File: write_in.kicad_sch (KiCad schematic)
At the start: 11 parts, among them J3 Bus_PCI_Express_x16, U30 74LS30, U31 74LS00, U32 74LS00

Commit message: Current progress.  Working on laying out the latched bus.
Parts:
- added C2: 100 nF, Capacitor_SMD:C_0805_2012Metric_Pad1.18x1.45mm_HandSolder, symbol Device:C
- added JP16: SolderJumper_3_Open, Jumper:SolderJumper-3_P1.3mm_Open_RoundedPad1.0x1.5mm, symbol Jumper:SolderJumper_3_Open
- added unit 2 of U3
- C1: renamed from C29; footprint (none) -> Capacitor_SMD:C_0805_2012Metric_Pad1.18x1.45mm_HandSolder
- C3: renamed from C30; footprint (none) -> Capacitor_SMD:C_0805_2012Metric_Pad1.18x1.45mm_HandSolder
- JP1: renamed from JP11; footprint (none) -> Jumper:SolderJumper-3_P1.3mm_Open_RoundedPad1.0x1.5mm
- JP2: renamed from JP12; footprint (none) -> Jumper:SolderJumper-3_P1.3mm_Open_RoundedPad1.0x1.5mm
- JP3: renamed from JP13; footprint (none) -> Jumper:SolderJumper-3_P1.3mm_Open_RoundedPad1.0x1.5mm
- JP4: renamed from JP14; footprint (none) -> Jumper:SolderJumper-3_P1.3mm_Open_RoundedPad1.0x1.5mm
- JP5: renamed from JP15; footprint (none) -> Jumper:SolderJumper-3_P1.3mm_Open_RoundedPad1.0x1.5mm
- U1: renamed from U31; footprint (none) -> Package_SO:SOIC-14_3.9x8.7mm_P1.27mm
- U2: renamed from U32; footprint (none) -> Package_SO:SOIC-14_3.9x8.7mm_P1.27mm
- U3: renamed from U30; footprint (none) -> Package_SO:SOIC-14_3.9x8.7mm_P1.27mm
- renumbered J3 to J1
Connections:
- net +3V3: now also C2.1, U3.14 (VCC)
- net GND: now also C2.2, JP16.1 (A), U3.7 (GND)
- net ~{RST}: now also JP16.3 (B)
- net write00 renamed write0
- net write01 renamed write1
- net write02 renamed write2
- net write03 renamed write3
- net write04 renamed write4
- net write05 renamed write5
- net write06 renamed write6
- net write07 renamed write7
- net write08 renamed write8
- net write09 renamed write9
- new net ~{ZRST}: JP16.2 (C)
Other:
- moved on the sheet: C1, C3, U1E, U2E

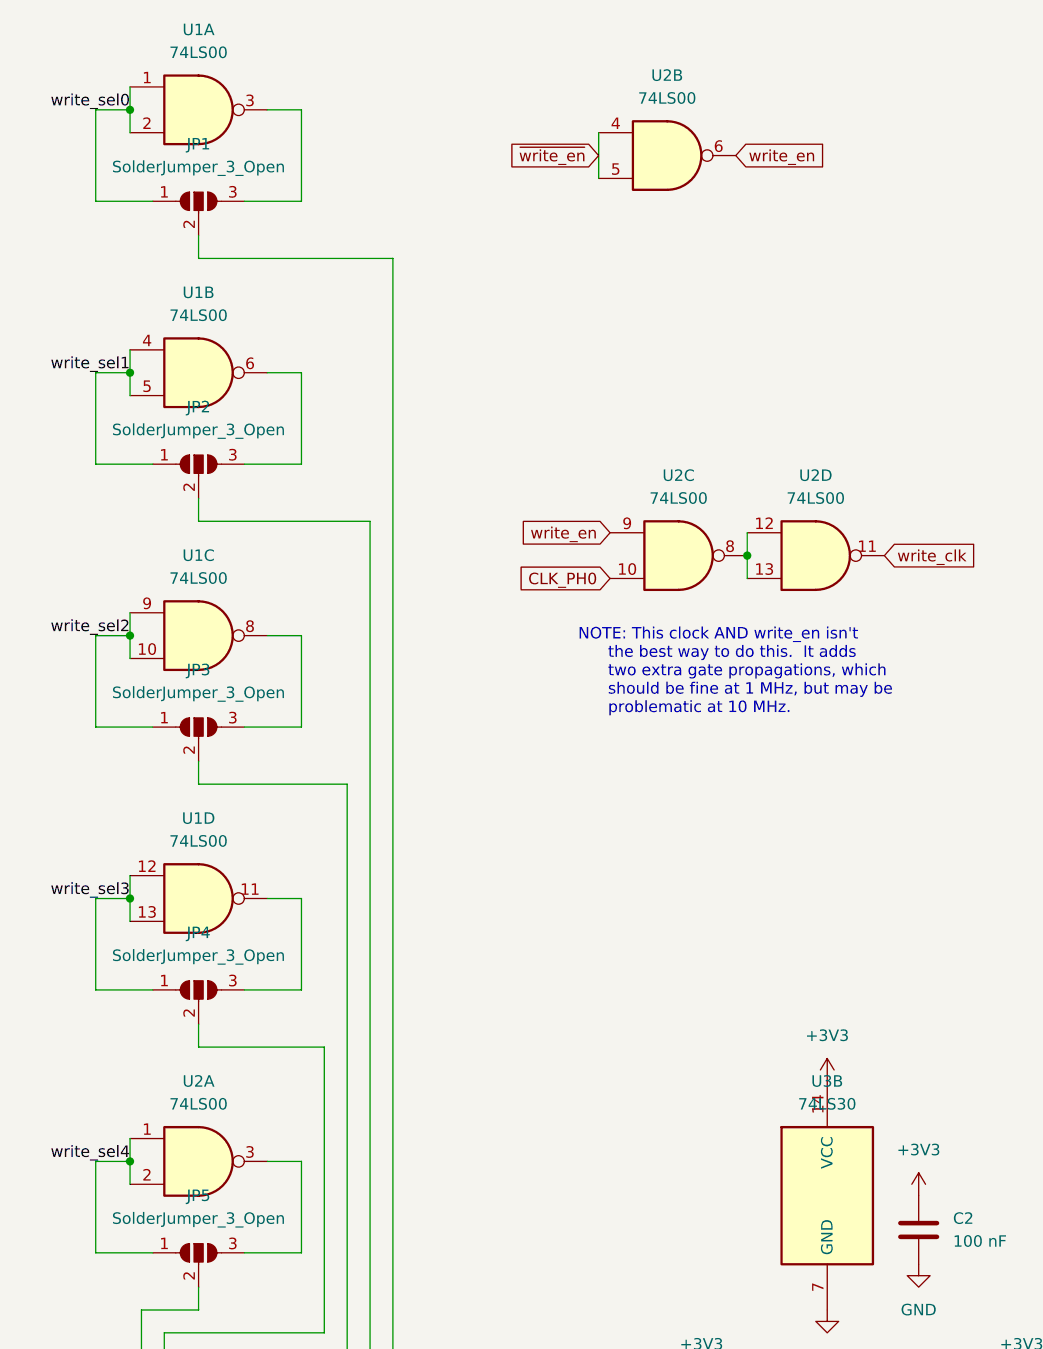
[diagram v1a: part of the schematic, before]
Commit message: Finished the register board layout.  It's not as short as I would have liked, but it's done.  64 bit busses take an amount of space.
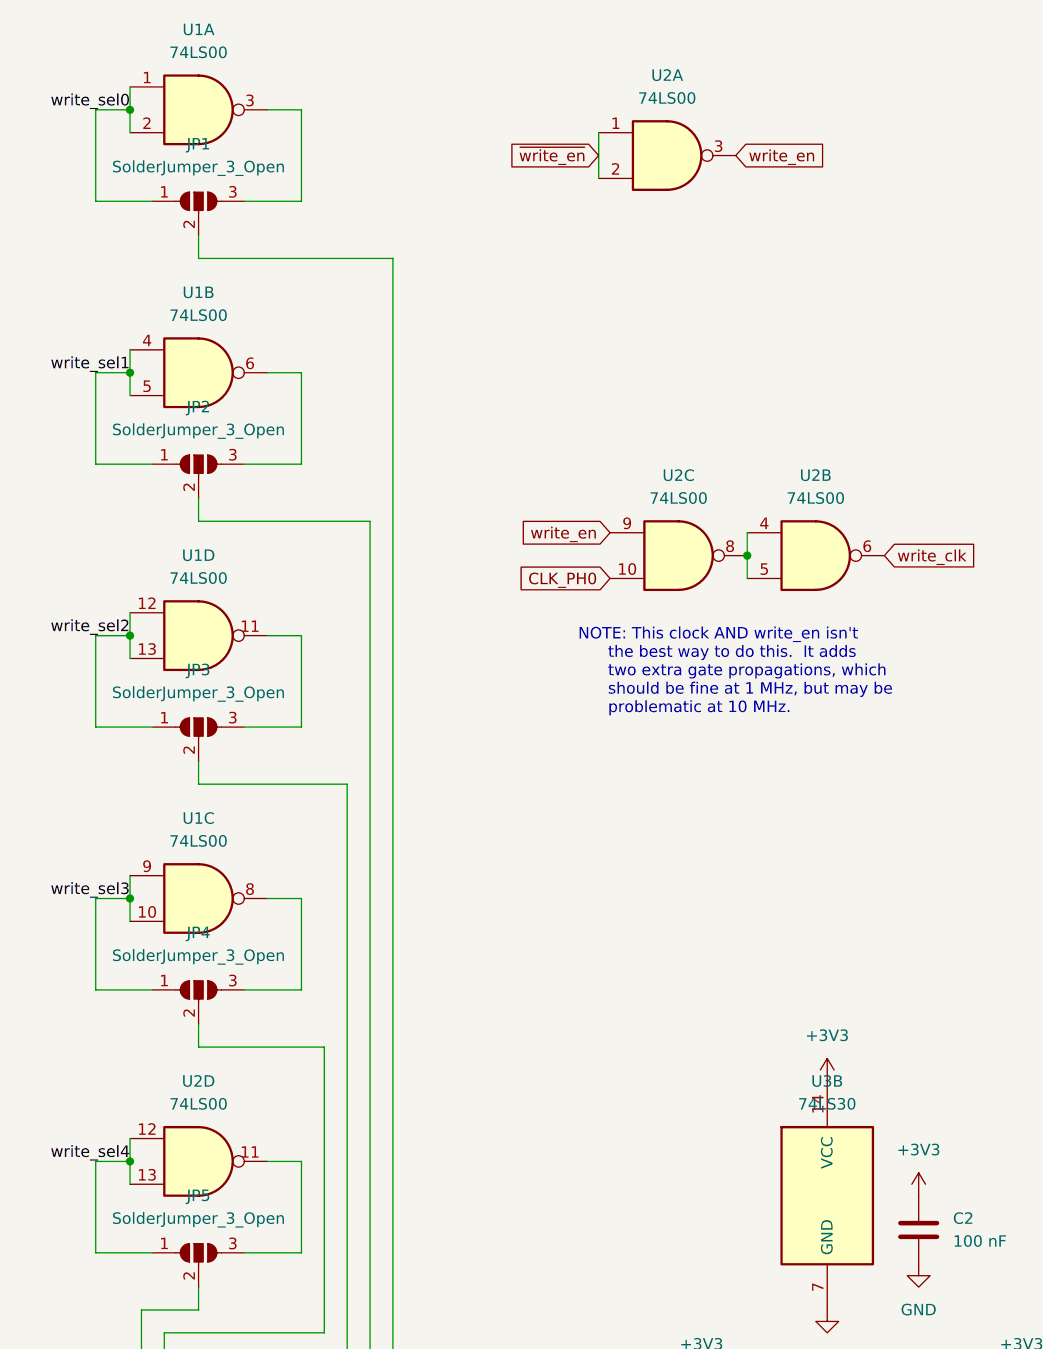
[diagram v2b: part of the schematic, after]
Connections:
- net write_clk: now also U2.6; no longer U2.11
- net write_en: now also U2.3; no longer U2.6
- net write_sel2: now also U1.12, U1.13; no longer U1.10, U1.9
- net write_sel3: now also U1.10, U1.9; no longer U1.12, U1.13
- net write_sel4: now also U2.12, U2.13; no longer U2.1, U2.2
- net ~{write_en}: now also U2.1, U2.2; no longer U2.4, U2.5
- net at JP4.3 (B): now also U1.8; no longer U1.11
- net at JP3.3 (B): now also U1.11; no longer U1.8
- net at JP5.3 (B): now also U2.11; no longer U2.3
- new net: U2.4, U2.5, U2.8
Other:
- moved on the sheet: U1C, U1D, U2A, U2B, U2D
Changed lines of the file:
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@@
 	(symbol
 		(lib_id "74xx:74LS00")
-		(at 110.49 72.39 0)
+		(at 41.91 139.7 0)
 		(unit 4)
 		(exclude_from_sim no)
@@
 		(fields_autoplaced yes)
 		(property "Reference" "U2"
-			(at 110.4817 63.5 0)
+			(at 41.9017 130.81 0)
 			(effects
 				(font
@@
 		)
 		(property "Value" "74LS00"
-			(at 110.4817 66.04 0)
+			(at 41.9017 133.35 0)
 			(effects
 				(font
@@
 		)
 		(property "Footprint" "Package_SO:SOIC-14_3.9x8.7mm_P1.27mm"
-			(at 110.49 72.39 0)
+			(at 41.91 139.7 0)
 			(effects
 				(font
@@
 		)
 		(property "Datasheet" "http://www.ti.com/lit/gpn/sn74ls00"
-			(at 110.49 72.39 0)
+			(at 41.91 139.7 0)
 			(effects
 				(font
@@
 		)
 		(property "Description" "quad 2-input NAND gate"
-			(at 110.49 72.39 0)
+			(at 41.91 139.7 0)
 			(effects
 				(font
@@
 	(symbol
 		(lib_id "74xx:74LS00")
-		(at 93.98 27.94 0)
+		(at 110.49 72.39 0)
 		(unit 2)
 		(exclude_from_sim no)
@@
 		(fields_autoplaced yes)
 		(property "Reference" "U2"
-			(at 93.9717 19.05 0)
+			(at 110.4817 63.5 0)
 			(effects
 				(font
@@
 		)
 		(property "Value" "74LS00"
-			(at 93.9717 21.59 0)
+			(at 110.4817 66.04 0)
 			(effects
 				(font
@@
 		)
 		(property "Footprint" "Package_SO:SOIC-14_3.9x8.7mm_P1.27mm"
-			(at 93.98 27.94 0)
+			(at 110.49 72.39 0)
 			(effects
 				(font
@@
 		)
 		(property "Datasheet" "http://www.ti.com/lit/gpn/sn74ls00"
-			(at 93.98 27.94 0)
+			(at 110.49 72.39 0)
 			(effects
 				(font
@@
 		)
 		(property "Description" "quad 2-input NAND gate"
-			(at 93.98 27.94 0)
+			(at 110.49 72.39 0)
 			(effects
 				(font
@@
 	(symbol
 		(lib_id "74xx:74LS00")
-		(at 41.91 81.28 0)
+		(at 41.91 110.49 0)
 		(unit 3)
 		(exclude_from_sim no)
@@
 		(fields_autoplaced yes)
 		(property "Reference" "U1"
-			(at 41.9017 72.39 0)
+			(at 41.9017 101.6 0)
 			(effects
 				(font
@@
 		)
 		(property "Value" "74LS00"
-			(at 41.9017 74.93 0)
+			(at 41.9017 104.14 0)
 			(effects
 				(font
@@
 		)
 		(property "Footprint" "Package_SO:SOIC-14_3.9x8.7mm_P1.27mm"
-			(at 41.91 81.28 0)
+			(at 41.91 110.49 0)
 			(effects
 				(font
@@
 		)
 		(property "Datasheet" "http://www.ti.com/lit/gpn/sn74ls00"
-			(at 41.91 81.28 0)
+			(at 41.91 110.49 0)
 			(effects
 				(font
@@
 		)
 		(property "Description" "quad 2-input NAND gate"
-			(at 41.91 81.28 0)
+			(at 41.91 110.49 0)
 			(effects
 				(font
@@
 	(symbol
 		(lib_id "74xx:74LS00")
-		(at 41.91 110.49 0)
+		(at 41.91 81.28 0)
 		(unit 4)
 		(exclude_from_sim no)
@@
 		(fields_autoplaced yes)
 		(property "Reference" "U1"
-			(at 41.9017 101.6 0)
+			(at 41.9017 72.39 0)
 			(effects
 				(font
@@
 		)
 		(property "Value" "74LS00"
-			(at 41.9017 104.14 0)
+			(at 41.9017 74.93 0)
 			(effects
 				(font
@@
 		)
 		(property "Footprint" "Package_SO:SOIC-14_3.9x8.7mm_P1.27mm"
-			(at 41.91 110.49 0)
+			(at 41.91 81.28 0)
 			(effects
 				(font
@@
 		)
 		(property "Datasheet" "http://www.ti.com/lit/gpn/sn74ls00"
-			(at 41.91 110.49 0)
+			(at 41.91 81.28 0)
 			(effects
 				(font
@@
 		)
 		(property "Description" "quad 2-input NAND gate"
-			(at 41.91 110.49 0)
+			(at 41.91 81.28 0)
 			(effects
 				(font
@@
 	(symbol
 		(lib_id "74xx:74LS00")
-		(at 41.91 139.7 0)
+		(at 93.98 27.94 0)
 		(unit 1)
 		(exclude_from_sim no)
@@
 		(fields_autoplaced yes)
 		(property "Reference" "U2"
-			(at 41.9017 130.81 0)
+			(at 93.9717 19.05 0)
 			(effects
 				(font
@@
 		)
 		(property "Value" "74LS00"
-			(at 41.9017 133.35 0)
+			(at 93.9717 21.59 0)
 			(effects
 				(font
@@
 		)
 		(property "Footprint" "Package_SO:SOIC-14_3.9x8.7mm_P1.27mm"
-			(at 41.91 139.7 0)
+			(at 93.98 27.94 0)
 			(effects
 				(font
@@
 		)
 		(property "Datasheet" "http://www.ti.com/lit/gpn/sn74ls00"
-			(at 41.91 139.7 0)
+			(at 93.98 27.94 0)
 			(effects
 				(font
@@
 		)
 		(property "Description" "quad 2-input NAND gate"
-			(at 41.91 139.7 0)
-			(effects
-				(font
+			(at 93.98 27.94 0)
+			(effects
+				(font
